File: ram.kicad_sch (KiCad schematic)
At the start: 7 parts

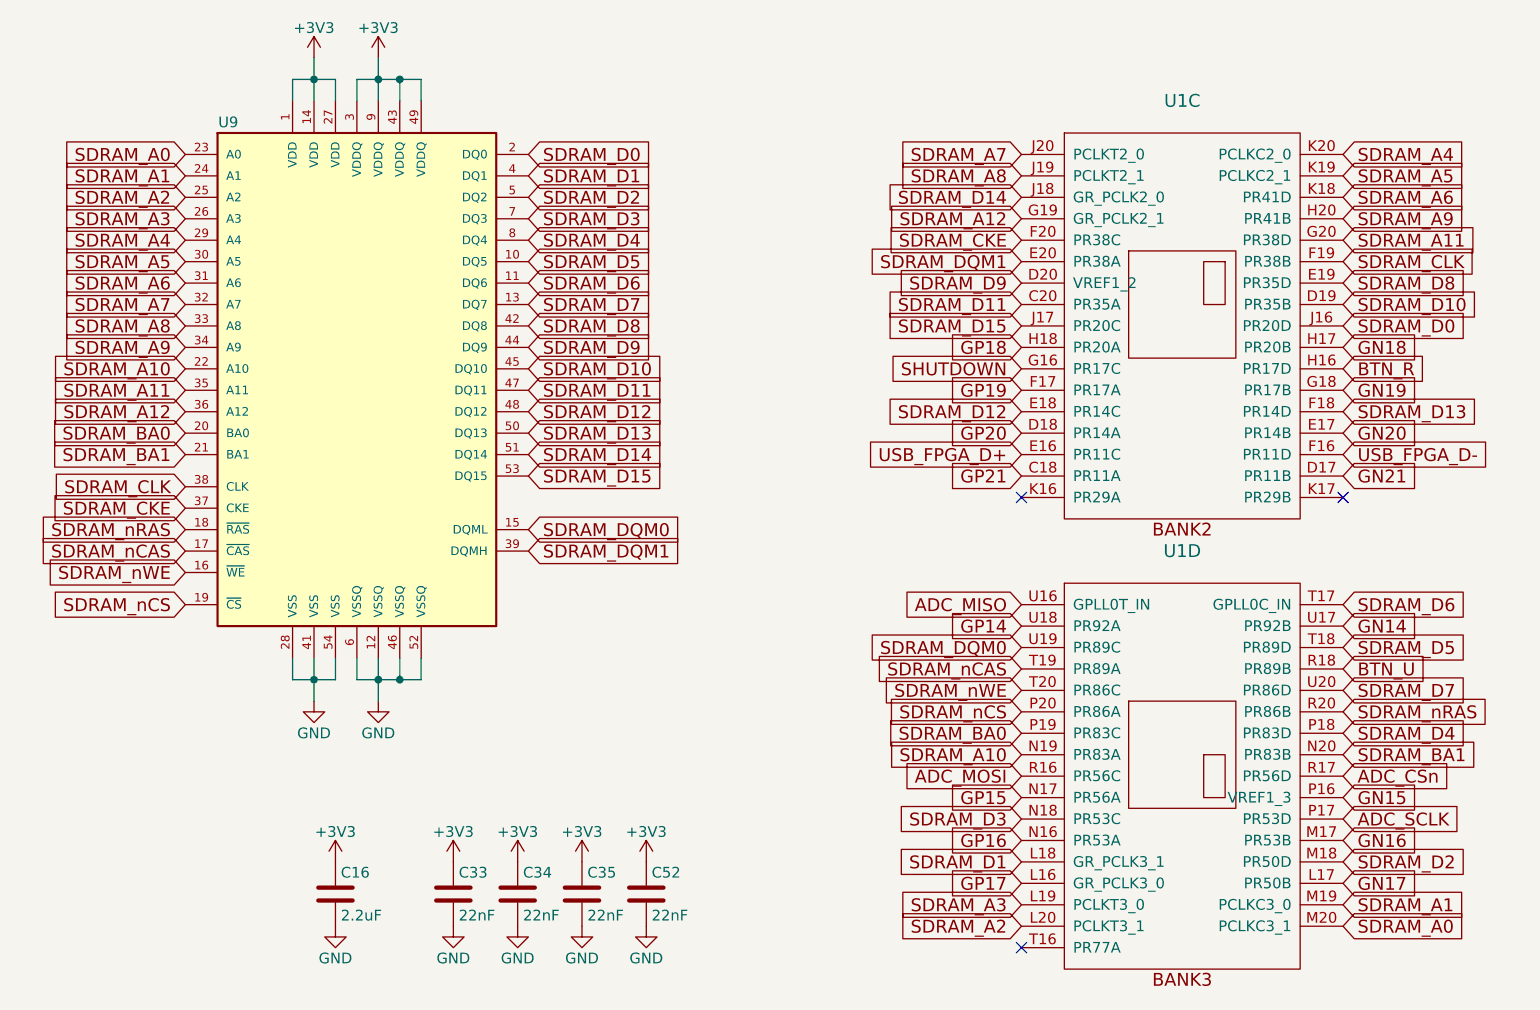
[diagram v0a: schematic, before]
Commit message: Adding USB-C
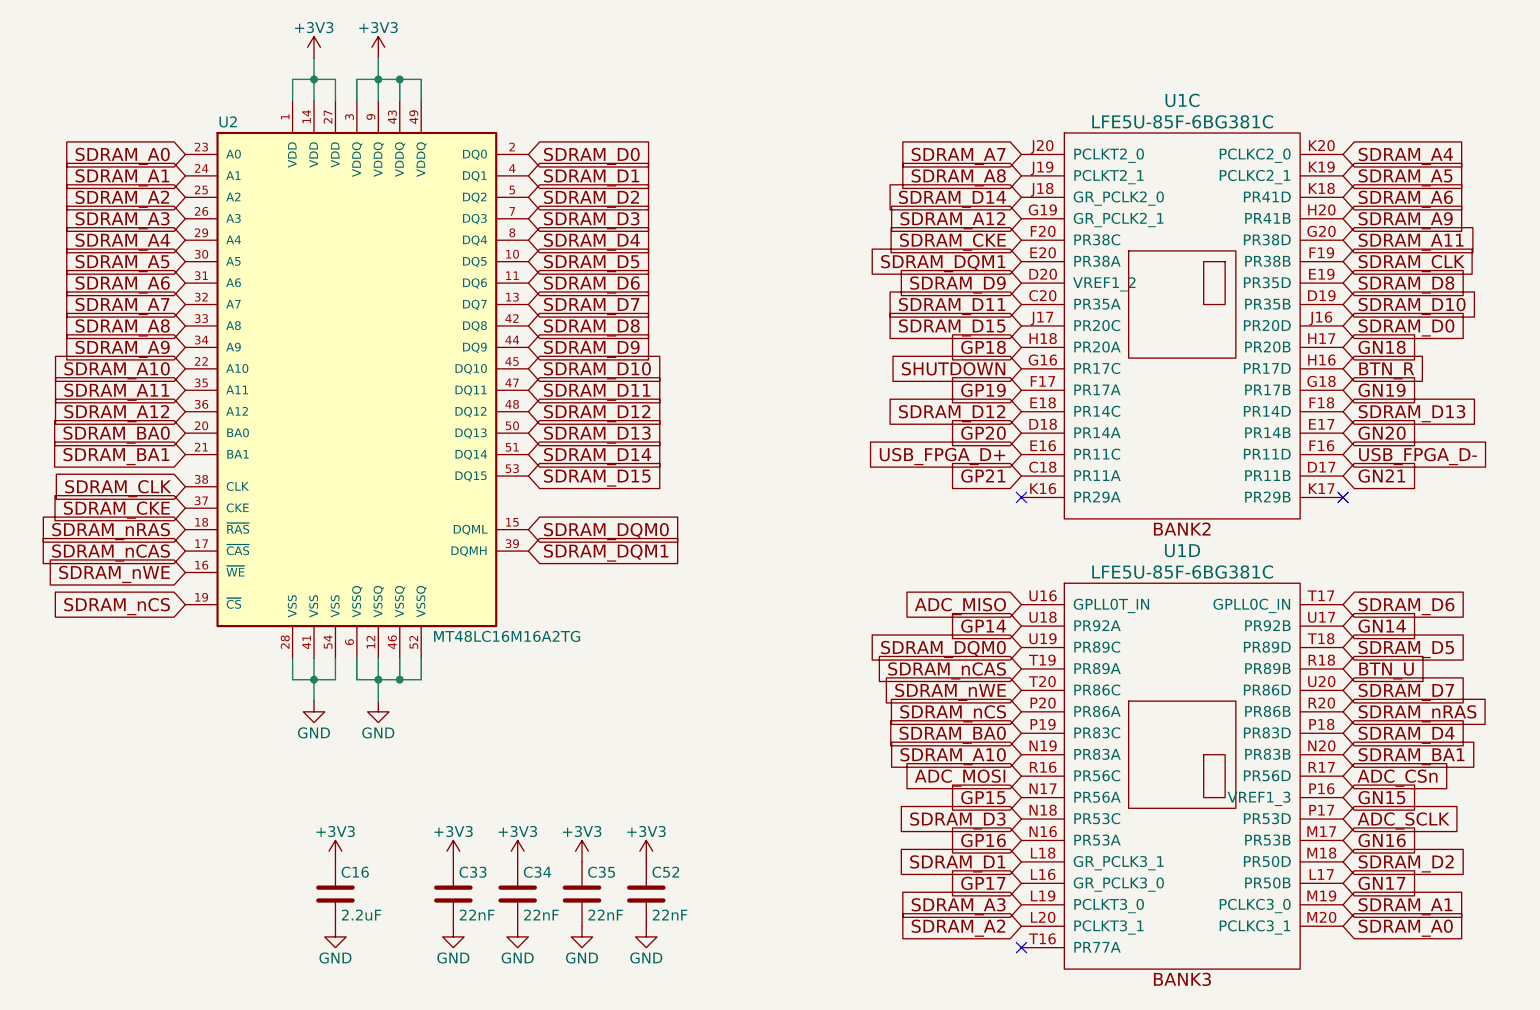
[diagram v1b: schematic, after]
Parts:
- U1: value (none) -> LFE5U-85F-6BG381C; footprint (none) -> lfe5bg381:BGA-381_pitch0.8mm_dia0.4mm
- U2: renamed from U9; value (none) -> MT48LC16M16A2TG; footprint (none) -> TSOP54:TSOP54
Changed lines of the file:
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@@
   (title_block
     (title "ULX3S")
-    (rev "1.0.0")
+    (date "2023-01-19")
+    (rev "3.1.8")
     (company "EMARD")
     (comment 1 "SDRAM memory")
@@
   (symbol (lib_id "mt48lc16m16a2tg:MT48LC16M16A2TG") (at 138.43 88.9 0) (unit 1)
     (in_bom yes) (on_board yes)
-    (property "Reference" "U9" (id 0) (at 123.19 58.42 0))
-    (property "Value" "" (id 1) (at 156.21 119.38 0))
-    (property "Footprint" "" (id 2) (at 138.43 88.9 0)
+    (property "Reference" "U2" (id 0) (at 123.19 58.42 0))
+    (property "Value" "MT48LC16M16A2TG" (id 1) (at 156.21 119.38 0))
+    (property "Footprint" "TSOP54:TSOP54" (id 2) (at 138.43 88.9 0)
       (effects (font (size 1.27 1.27) italic) hide)
     )
@@
       (effects (font (size 1.524 1.524)))
     )
-    (property "Value" "" (id 1) (at 236.22 58.42 0)
+    (property "Value" "LFE5U-85F-6BG381C" (id 1) (at 236.22 58.42 0)
       (effects (font (size 1.524 1.524)))
     )
-    (property "Footprint" "" (id 2) (at 209.55 55.88 0)
+    (property "Footprint" "lfe5bg381:BGA-381_pitch0.8mm_dia0.4mm" (id 2) (at 209.55 55.88 0)
       (effects (font (size 1.524 1.524)) hide)
     )
@@
       (effects (font (size 1.524 1.524)))
     )
-    (property "Value" "" (id 1) (at 236.22 111.76 0)
+    (property "Value" "LFE5U-85F-6BG381C" (id 1) (at 236.22 111.76 0)
       (effects (font (size 1.524 1.524)))
     )
-    (property "Footprint" "" (id 2) (at 209.55 109.22 0)
+    (property "Footprint" "lfe5bg381:BGA-381_pitch0.8mm_dia0.4mm" (id 2) (at 209.55 109.22 0)
       (effects (font (size 1.524 1.524)) hide)
     )
